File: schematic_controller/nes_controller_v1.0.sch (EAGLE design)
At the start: 22 parts

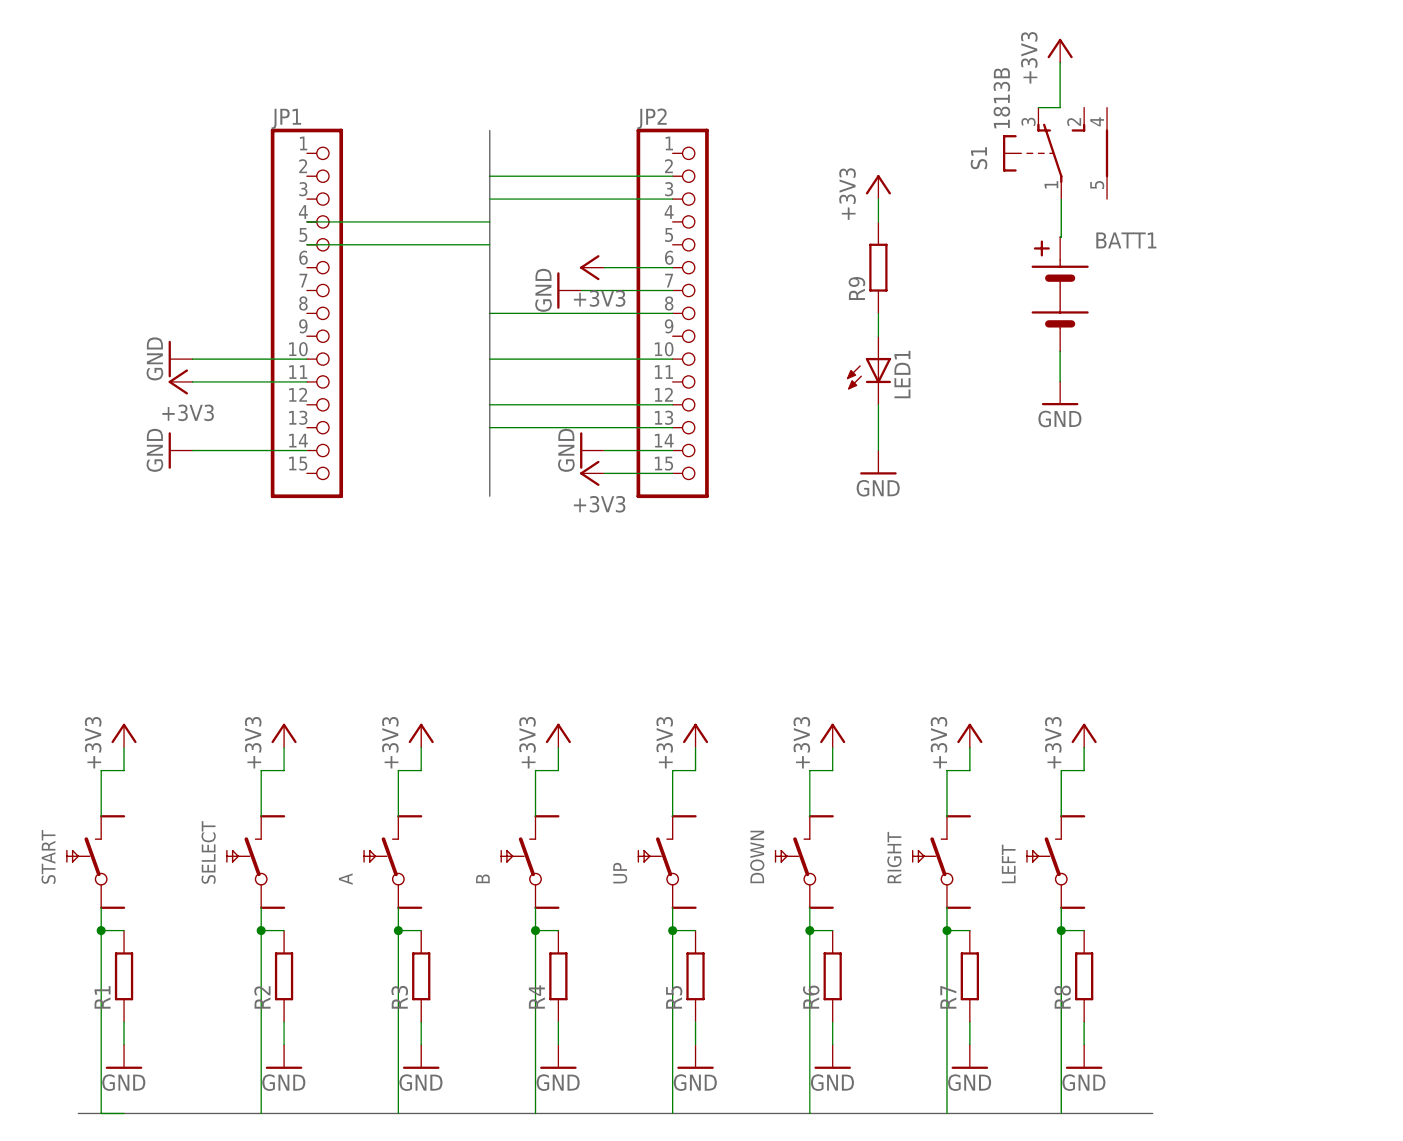
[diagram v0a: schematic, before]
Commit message: updated schematic with debounced buttons
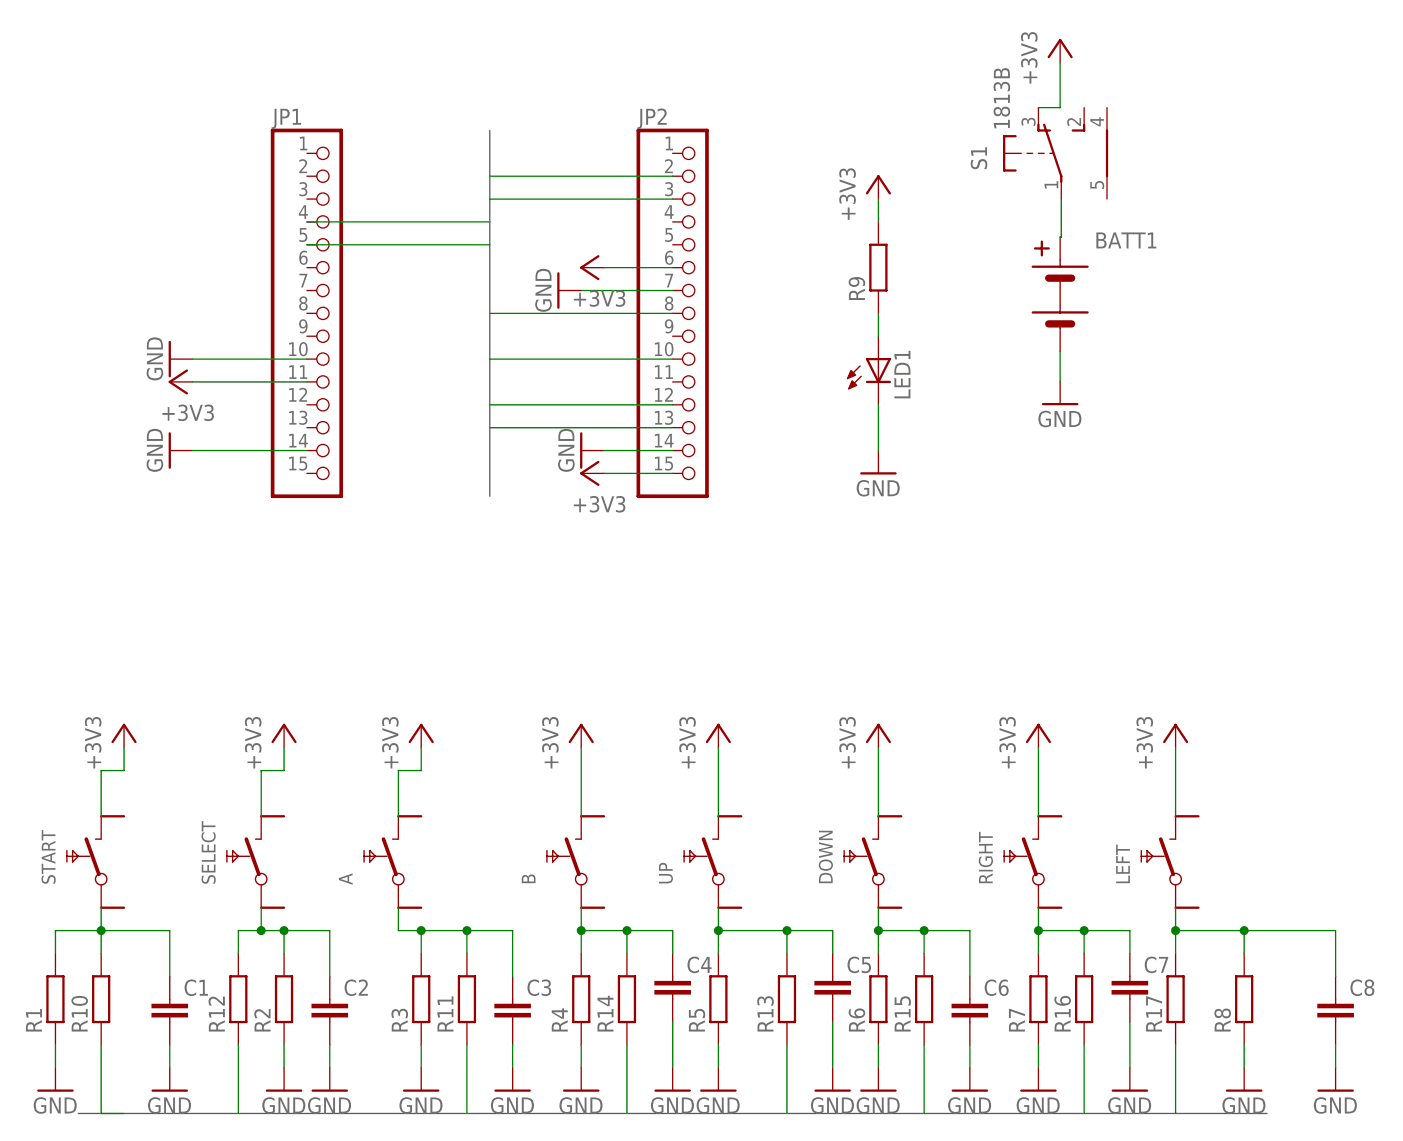
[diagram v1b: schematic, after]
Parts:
- added C1, C2, C3, C4, C5, C6, C7, C8: (no value), rcl:C-EUC0805K
- added R10, R11, R12, R13, R14, R15, R16, R17: (no value), rcl:R-EU_MELF0207R
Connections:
- new net 3§4: C2.1, R12.2, R2.2, SELECT.1
- new net 4$5: A.1, C3.1, R11.2, R3.2
- new net N$3: C1.1, R1.2, R10.2, START.1
- new net N$4: B.1, C4.1, R14.2, R4.2
- new net N$5: C5.1, R13.2, R5.2, UP.1
- new net N$6: C6.1, DOWN.1, R15.2, R6.2
- new net N$7: C7.1, R16.2, R7.2, RIGHT.1
- new net N$8: C8.1, LEFT.1, R17.2, R8.2
- net A: now also R11.1; no longer A.1, R3.2
- net B: now also R14.1; no longer B.1, R4.2
- net DOWN: now also R15.1; no longer DOWN.1, R6.2
- net GND: now also C1.2, C2.2, C3.2, C4.2, C5.2, C6.2, C7.2, C8.2
- net LEFT: now also R17.1; no longer LEFT.1, R8.2
- net RIGHT: now also R16.1; no longer R7.2, RIGHT.1
- net SELECT: now also R12.1; no longer R2.2, SELECT.1
- net START: now also R10.1; no longer R1.2, START.1
- net UP: now also R13.1; no longer R5.2, UP.1
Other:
- moved on the sheet: B, DOWN, LEFT, R1, R2, R3, R4, R5, R6, R7, R8, RIGHT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
